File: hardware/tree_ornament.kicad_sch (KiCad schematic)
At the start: 21 parts, among them J1 Conn_02x03_Counter_Clockwise, SW1 TL1107BF130WQ, U1 ATtiny85-20P

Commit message: Added silkscreen/edge cuts, placed footprints, initial release
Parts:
- U1: footprint Package_DIP:DIP-8_W7.62mm -> tree_ornament:SOIC127P798X216-8N
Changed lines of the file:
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@@
 			)
 		)
-		(property "Footprint" "Package_DIP:DIP-8_W7.62mm"
+		(property "Footprint" "tree_ornament:SOIC127P798X216-8N"
 			(at 113.03 83.82 0)
 			(effects

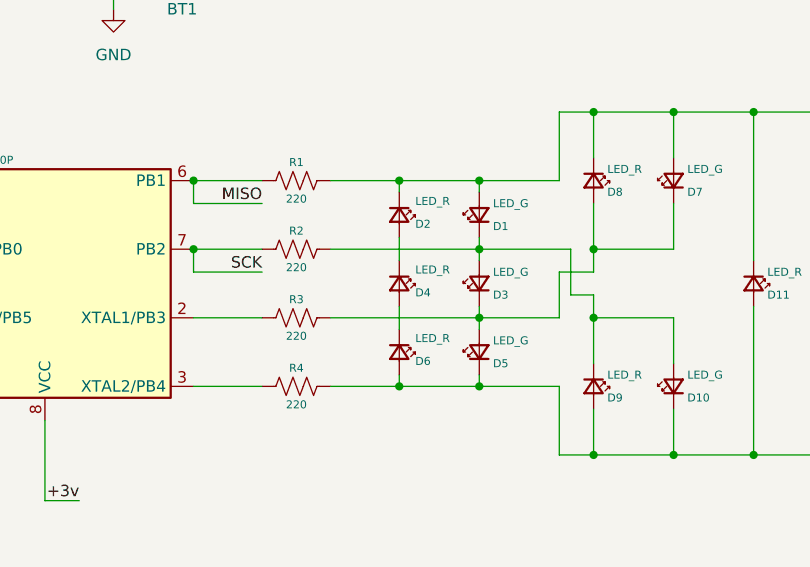
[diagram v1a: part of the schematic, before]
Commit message: Found unconnected LEDs, cleaned up firmware code
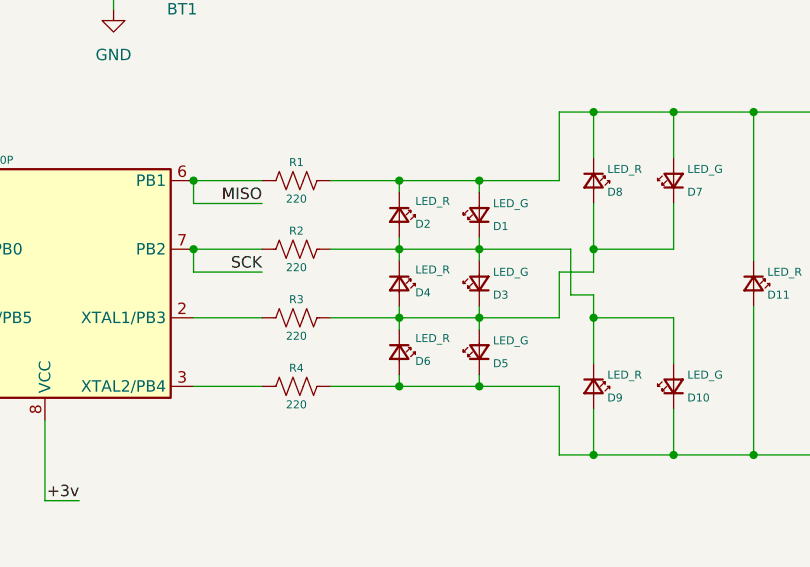
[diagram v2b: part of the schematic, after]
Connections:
- net at D1.1 (K), D10.2 (A), D3.2 (A)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: now also D2.2 (A), D4.1 (K)
- net at D4.2 (A), D6.1 (K): now also D3.1 (K), D5.2 (A), D7.1 (K), D8.2 (A), R3.1
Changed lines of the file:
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@@
+	)
+	(junction
+		(at 151.13 87.63)
+		(diameter 0)
+		(color 0 0 0 0)
 	)
 	(junction
@@
 	)
 	(junction
+		(at 151.13 80.01)
+		(diameter 0)
+		(color 0 0 0 0)
+	)
+	(junction
 		(at 172.72 102.87)
 		(diameter 0)
@@
 	(wire
 		(pts
-			(xy 151.13 81.28) (xy 151.13 78.74)
+			(xy 151.13 81.28) (xy 151.13 80.01)
 		)
 		(stroke
@@
 	(wire
 		(pts
+			(xy 151.13 87.63) (xy 160.02 87.63)
+		)
+		(stroke
+			(width 0)
+			(type default)
+		)
+	)
+	(wire
+		(pts
 			(xy 170.18 80.01) (xy 170.18 85.09)
 		)
@@
 	(wire
 		(pts
-			(xy 143.51 87.63) (xy 160.02 87.63)
-		)
-		(stroke
-			(width 0)
-			(type default)
-		)
-	)
-	(wire
-		(pts
 			(xy 118.11 130.81) (xy 123.19 130.81)
 		)
@@
 	(wire
 		(pts
+			(xy 151.13 80.01) (xy 151.13 78.74)
+		)
+		(stroke
+			(width 0)
+			(type default)
+		)
+	)
+	(wire
+		(pts
 			(xy 160.02 80.01) (xy 170.18 80.01)
 		)
@@
 	(wire
 		(pts
-			(xy 143.51 80.01) (xy 160.02 80.01)
-		)
-		(stroke
-			(width 0)
-			(type default)
-		)
-	)
-	(wire
-		(pts
 			(xy 128.27 87.63) (xy 135.89 87.63)
 		)
@@
 	(wire
 		(pts
+			(xy 143.51 87.63) (xy 151.13 87.63)
+		)
+		(stroke
+			(width 0)
+			(type default)
+		)
+	)
+	(wire
+		(pts
 			(xy 123.19 125.73) (xy 118.11 125.73)
 		)
@@
 	(wire
 		(pts
-			(xy 151.13 88.9) (xy 151.13 86.36)
-		)
-		(stroke
-			(width 0)
-			(type default)
-		)
-	)
-	(wire
-		(pts
 			(xy 100.33 130.81) (xy 105.41 130.81)
 		)
@@
 	(wire
 		(pts
+			(xy 143.51 80.01) (xy 151.13 80.01)
+		)
+		(stroke
+			(width 0)
+			(type default)
+		)
+	)
+	(wire
+		(pts
 			(xy 151.13 93.98) (xy 151.13 95.25)
 		)
@@
 	(wire
 		(pts
+			(xy 151.13 80.01) (xy 160.02 80.01)
+		)
+		(stroke
+			(width 0)
+			(type default)
+		)
+	)
+	(wire
+		(pts
 			(xy 160.02 95.25) (xy 168.91 95.25)
 		)
@@
 	(wire
 		(pts
+			(xy 151.13 87.63) (xy 151.13 88.9)
+		)
+		(stroke
+			(width 0)
+			(type default)
+		)
+	)
+	(wire
+		(pts
 			(xy 181.61 74.93) (xy 181.61 80.01)
 		)
@@
 		)
 		(stroke
+			(width 0)
+			(type default)
+		)
+	)
+	(wire
+		(pts
+			(xy 151.13 86.36) (xy 151.13 87.63)
+		)
+		(stroke

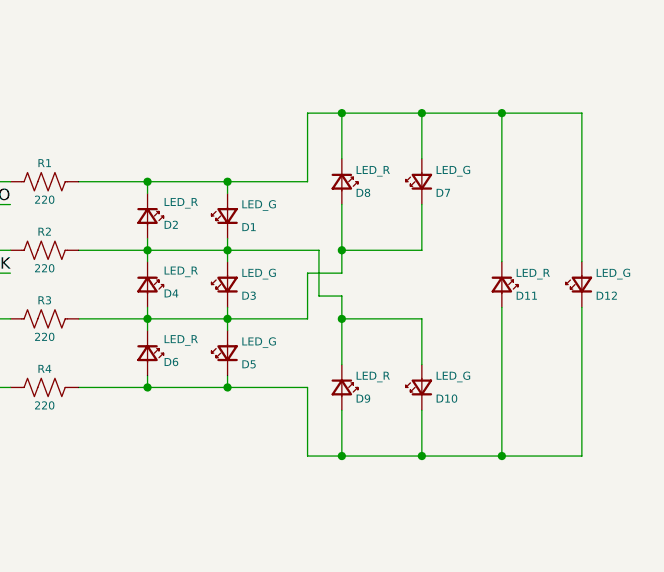
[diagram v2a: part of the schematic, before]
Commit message: Fixed swapped pins
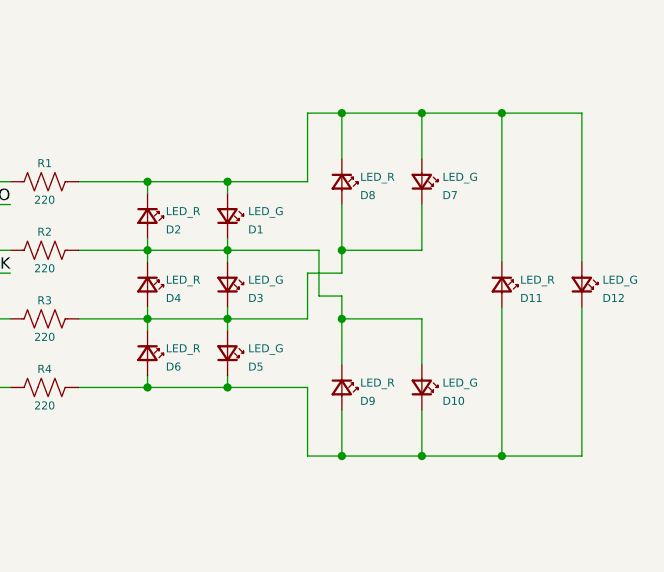
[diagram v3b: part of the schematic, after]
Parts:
- removed D1, D10, D12, D3, D5, D7: LED_G, tree_ornament:WL-TMRC_3MM_LED, symbol Device:LED_Small
- removed D11, D2, D4, D6, D8, D9: LED_R, tree_ornament:WL-TMRC_3MM_LED, symbol Device:LED_Small
- added D1, D10, D12, D3, D5, D7: LED_G, tree_ornament:WL-TMRC_3MM_LED, symbol ornament_small_led:LED_Small
- added D11, D2, D4, D6, D8, D9: LED_R, tree_ornament:WL-TMRC_3MM_LED, symbol ornament_small_led:LED_Small
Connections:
- net at R4.1: now also D10.2 (K), D11.1 (A), D12.2 (K), D5.2 (K), D6.1 (A), D9.1 (A)
- net at R2.1: now also D1.2 (K), D10.1 (A), D2.1 (A), D3.1 (A), D4.2 (K), D9.2 (K)
- net at R3.1: now also D3.2 (K), D4.1 (A), D5.1 (A), D6.2 (K), D7.2 (K), D8.1 (A)
- net at R1.1: now also D1.1 (A), D11.2 (K), D12.1 (A), D2.2 (K), D7.1 (A), D8.2 (K)
